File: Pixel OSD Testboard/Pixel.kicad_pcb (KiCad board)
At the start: 2 copper layers, 35 x 35 mm, 144 parts, among them J1 USB_C_Receptacle_USB2.0_16P, Q1 2SK3019, U1 RP2040, U10 FSA3157P6X, U11 Opamp_Quad, U2 LM1881, U3 W25Q16JVSS, U4 Opamp_Quad, U5 74LVC1G66, U6 FSA3157P6X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

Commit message: ^wip layout
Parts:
- U11: value Opamp_Quad -> OPA188xxDBV; footprint Package_SO:TSSOP-14_4.4x5mm_P0.65mm -> Package_TO_SOT_SMD:TSOT-23-5
- moved C29 86.7 mm to (95.0, 82.0)
- moved C30 86.7 mm to (95.0, 83.8)
- moved C31 86.7 mm to (95.0, 85.5)
- moved C32 86.7 mm to (95.0, 87.2)
- moved C33 86.7 mm to (95.0, 89.0)
- moved C34 86.7 mm to (95.0, 90.8)
- moved C35 86.7 mm to (95.0, 92.5)
- moved C36 86.7 mm to (95.0, 94.2)
- moved C52 85.3 mm to (106.2, 84.0)
- moved R26 85.0 mm to (106.2, 94.2), turned to -90 degrees
- moved R22 82.5 mm to (106.2, 87.2), turned to -90 degrees
- moved R24 82.1 mm to (106.2, 90.8), turned to -90 degrees
- moved R23 80.9 mm to (107.8, 89.0), turned to -90 degrees
- moved R25 80.4 mm to (107.8, 92.5), turned to -90 degrees
- moved C18 80.4 mm to (110.2, 76.0), turned to -90 degrees
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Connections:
- R43 pad 2: Net-(U11A--) -> Net-(U11--)
- R44 pad 1: Net-(U11A--) -> Net-(U11--)
- TP8 pad 1: /BLACK_ADC -> /BLACK_SAH
- U11 pad 2: Net-(U11A--) -> GND
- U11 pad 4: +5V -> Net-(U11--)
- U11 pad 5: unconnected-(U11B-+-Pad5) -> +5V

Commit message: layout done?
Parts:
- moved C37 33.3 mm to (109.5, 71.2), turned to -90 degrees
- moved C38 33.2 mm to (110.2, 71.2), turned to -90 degrees
- moved C39 32.8 mm to (111.5, 71.2), turned to -90 degrees
- moved C40 32.7 mm to (112.5, 71.2), turned to -90 degrees
- moved C44 25.3 mm to (128.0, 72.5), turned to -90 degrees
- moved C43 24.4 mm to (127.0, 72.5), turned to -90 degrees
- moved C42 23.9 mm to (125.5, 72.5), turned to -90 degrees
- moved C41 23.2 mm to (124.8, 72.5), turned to -90 degrees
- moved C29 13.1 mm to (104.0, 91.5)
- moved C30 12.6 mm to (104.0, 92.5)
- moved C31 12.2 mm to (104.0, 93.8)
- moved C32 11.6 mm to (104.0, 94.5)
- moved C36 11.3 mm to (103.5, 86.8)
- moved C35 10.7 mm to (103.5, 86.0)
- moved C34 8.56 mm to (103.5, 89.8)
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
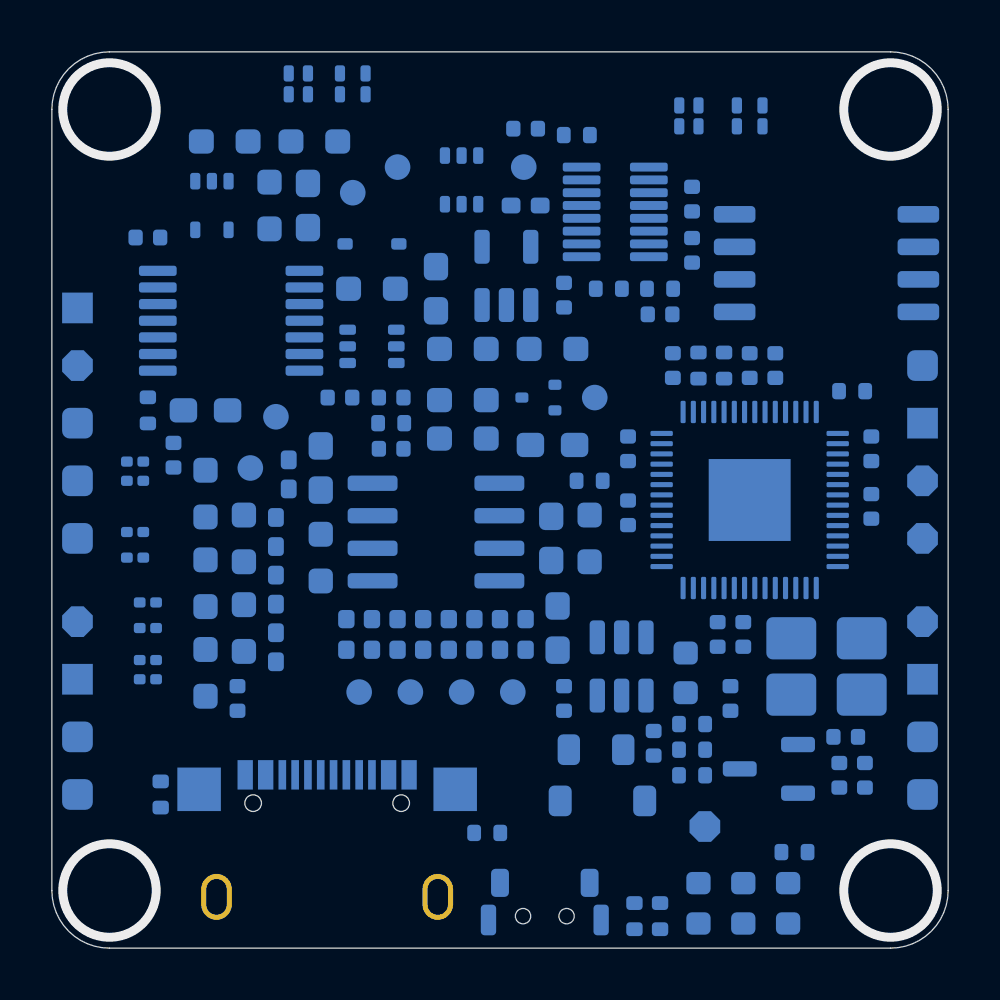
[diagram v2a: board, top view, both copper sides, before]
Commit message: 0 DRC errors
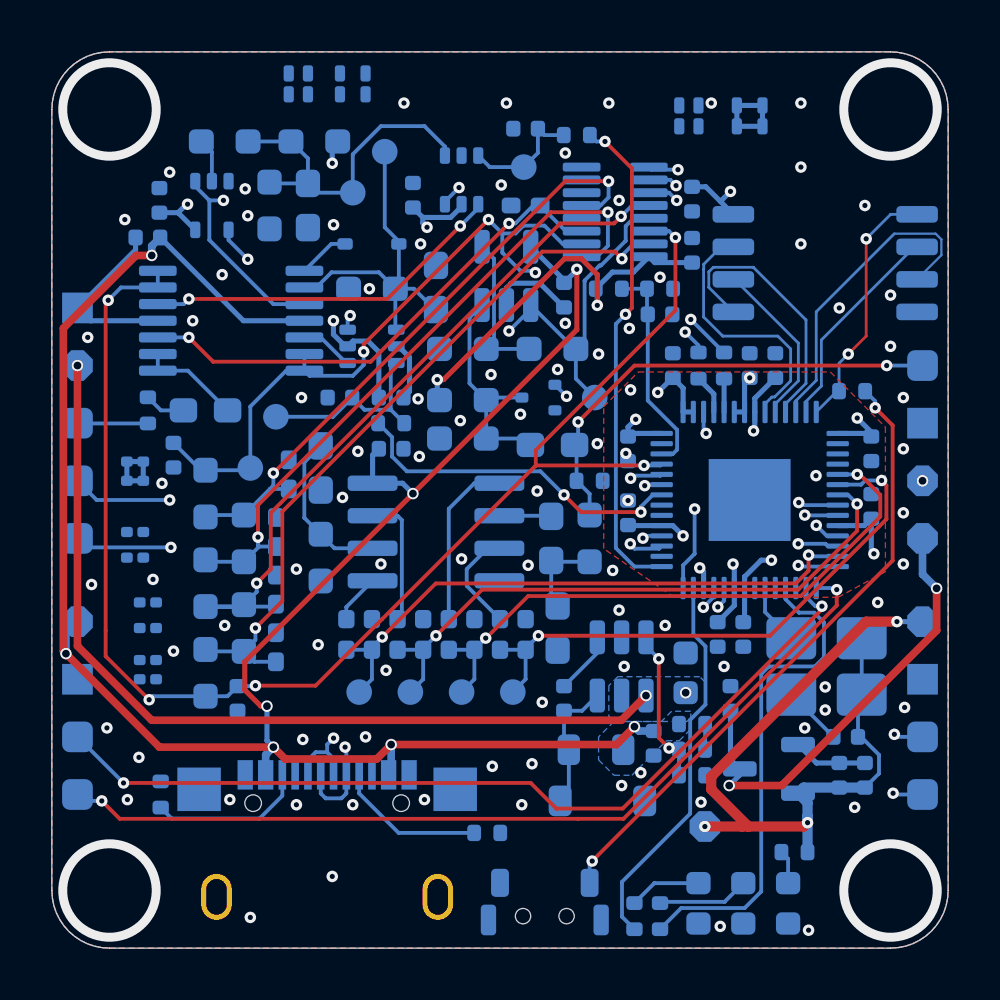
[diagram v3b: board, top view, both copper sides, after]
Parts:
- added C56: 100n, Capacitor_SMD:C_0402_1005Metric, B.Cu at (114.3, 75.6)
- added C57: 100n, Capacitor_SMD:C_0402_1005Metric, B.Cu at (104.5, 75.8)
- moved TP5 0.78 mm to (113.2, 73.9)
- moved U3 0.05 mm to (130.4, 78.2)
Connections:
- U1 pad 18: /LED1 -> /LED2
- U1 pad 27: /LED2 -> /LED1
- U1 pad 3: /VWHITE_PWM -> unconnected-(U1-GPIO1-Pad3)
- U1 pad 36: unconnected-(U1-GPIO24-Pad36) -> /VWHITE_PWM
- U1 pad 37: unconnected-(U1-GPIO25-Pad37) -> /WHITE_SELECT
- U1 pad 4: /WHITE_SELECT -> unconnected-(U1-GPIO2-Pad4)
- U10 pad 2: (no net) -> GND
- U10 pad 5: (no net) -> +3V3
- U5 pad 3: (no net) -> GND
- U5 pad 5: (no net) -> +3V3
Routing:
- net +3V3: track 0.00 -> 124.7 mm, vias 0 -> 19
- net +5V: track 0.00 -> 107.1 mm, vias 0 -> 10
- net +10V: track 0.00 -> 60.1 mm, vias 0 -> 4
- net /BLACK_ADC: track 0.00 -> 55.3 mm, vias 0 -> 5
- net /WHITE_ADC: track 0.00 -> 37.9 mm, vias 0 -> 4
- net /TX0: track 0.00 -> 34.9 mm, vias 0 -> 2
- net /RX0: track 0.00 -> 34.7 mm, vias 0 -> 2
- net /VIDEO_IN_CLAMP: track 0.00 -> 33.8 mm, vias 0 -> 2
- net /BLACK_CHG: track 0.00 -> 29.2 mm, vias 0 -> 2
- net /GREY2: track 0.00 -> 28.1 mm, vias 0 -> 2
- net /GREY1: track 0.00 -> 28.0 mm, vias 0 -> 2
- net Net-(J1-D+-PadA6): track 0.00 -> 27.8 mm, vias 0 -> 2
- net Net-(J1-D--PadA7): track 0.00 -> 27.2 mm, vias 0 -> 2
- net /GREY3: track 0.00 -> 25.6 mm, vias 0 -> 2
- net Net-(R15-Pad1): track 0.00 -> 24.5 mm, vias 0 -> 2
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- added copper zone on B.Cu, net +10V
- added copper zone on In2.Cu, net +1V1
- added copper zone on F.Cu, net +3V3
- added copper zone on B.Cu, net +5V
- added copper zone on B.Cu, net GND
- added copper zone on F.Cu, net GND
- added copper zone on In1.Cu, net GND
- added copper zone on In2.Cu, net GND
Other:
- copper layers 2 -> 4

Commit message: upgrade to 6 layers for free POFV and free thinner
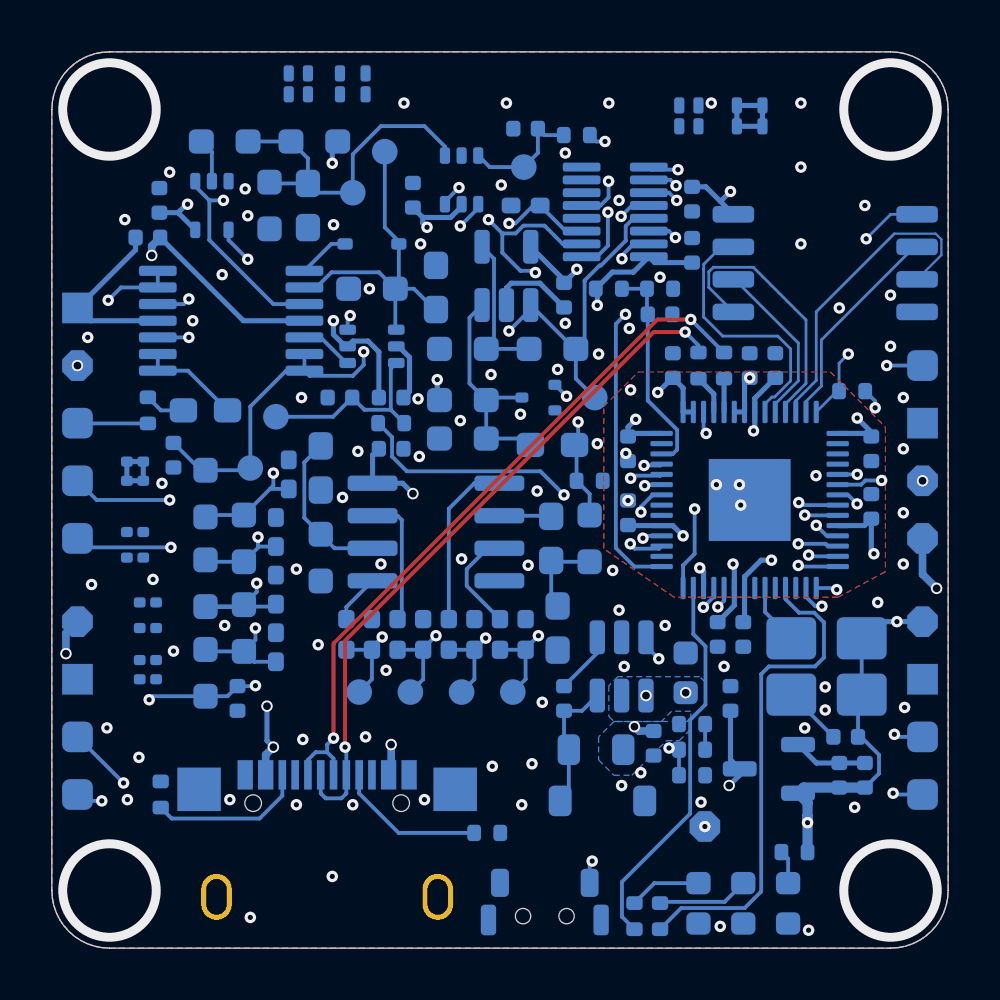
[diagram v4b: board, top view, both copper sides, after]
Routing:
- net GND: vias 92 -> 95
- added copper zone on In3.Cu, net +1V1
- added copper zone on In3.Cu, net GND
- added copper zone on In4.Cu, net GND
- removed copper zone on In2.Cu, net +1V1
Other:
- copper layers 4 -> 6

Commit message: some silkscreen
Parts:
- removed TP7: TestPoint_Probe, TestPoint:TestPoint_Pad_D1.0mm
- moved TP8 4.58 mm to (114.7, 71.8)
- moved C55 0.71 mm to (119.2, 72.5), turned to 90 degrees
- moved C45 0.07 mm to (125.2, 77.8)
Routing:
- net +10V: track 60.1 -> 50.9 mm
- net /WHITE_ADC: track 37.9 -> 36.9 mm
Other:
- board text added: "10V"
- board text added: "3V3"
- board text added: "5V"
- board text added: "BOOT"
- board text added: "BPo"
- board text added: "GND"
- board text added: "Odd"
- board text added: "R0"
- board text added: "R1"
- board text added: "SBl"
- board text added: "SWC"
- board text added: "SWD"
- board text added: "SWh"
- board text added: "Syn"
- board text added: "T0"
- board text added: "T1"
- board text added: "VBl"
- board text added: "VI"
- board text added: "VO"
- board text added: "VSy"
- board text added: "VWh"
- board text added: "VinC"

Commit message: as ordered
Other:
- board text added: "Analog FTW!"
- board text added: "Pixel OSD V1"
- board text added: "https://github.com/bastian2001/Kolibri-FC-Hardware"
